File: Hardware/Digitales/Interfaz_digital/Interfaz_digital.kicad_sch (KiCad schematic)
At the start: 47 parts, among them J0_1 Screw_Terminal_01x03, J0_2 Screw_Terminal_01x03, J0_3 Screw_Terminal_01x03, J1-1 Screw_Terminal_01x01, J1-2 Screw_Terminal_01x01, J2-1 Screw_Terminal_01x01, J2-2 Screw_Terminal_01x01, J3-1 Screw_Terminal_01x01, J3-2 Screw_Terminal_01x01, J4-1 Screw_Terminal_01x01, J4-2 Screw_Terminal_01x01, J5-1 Screw_Terminal_01x01, J5-2 Screw_Terminal_01x01, J6-1 Screw_Terminal_01x01, J6-2 Screw_Terminal_01x01, J7-1 Screw_Terminal_01x01, J7-2 Screw_Terminal_01x01, J8-1 Screw_Terminal_01x01, J8-2 Screw_Terminal_01x01, J9_1 Screw_Terminal_01x03, J9_2 Screw_Terminal_01x03, J9_3 Screw_Terminal_01x03, J9_4 Screw_Terminal_01x03, U1 TLP521-1, U2 TLP521-1, U3 TLP521-1, U4 TLP521-1, U5 TLP521-1, U6 TLP521-1, U7 TLP521-1, U8 TLP521-1

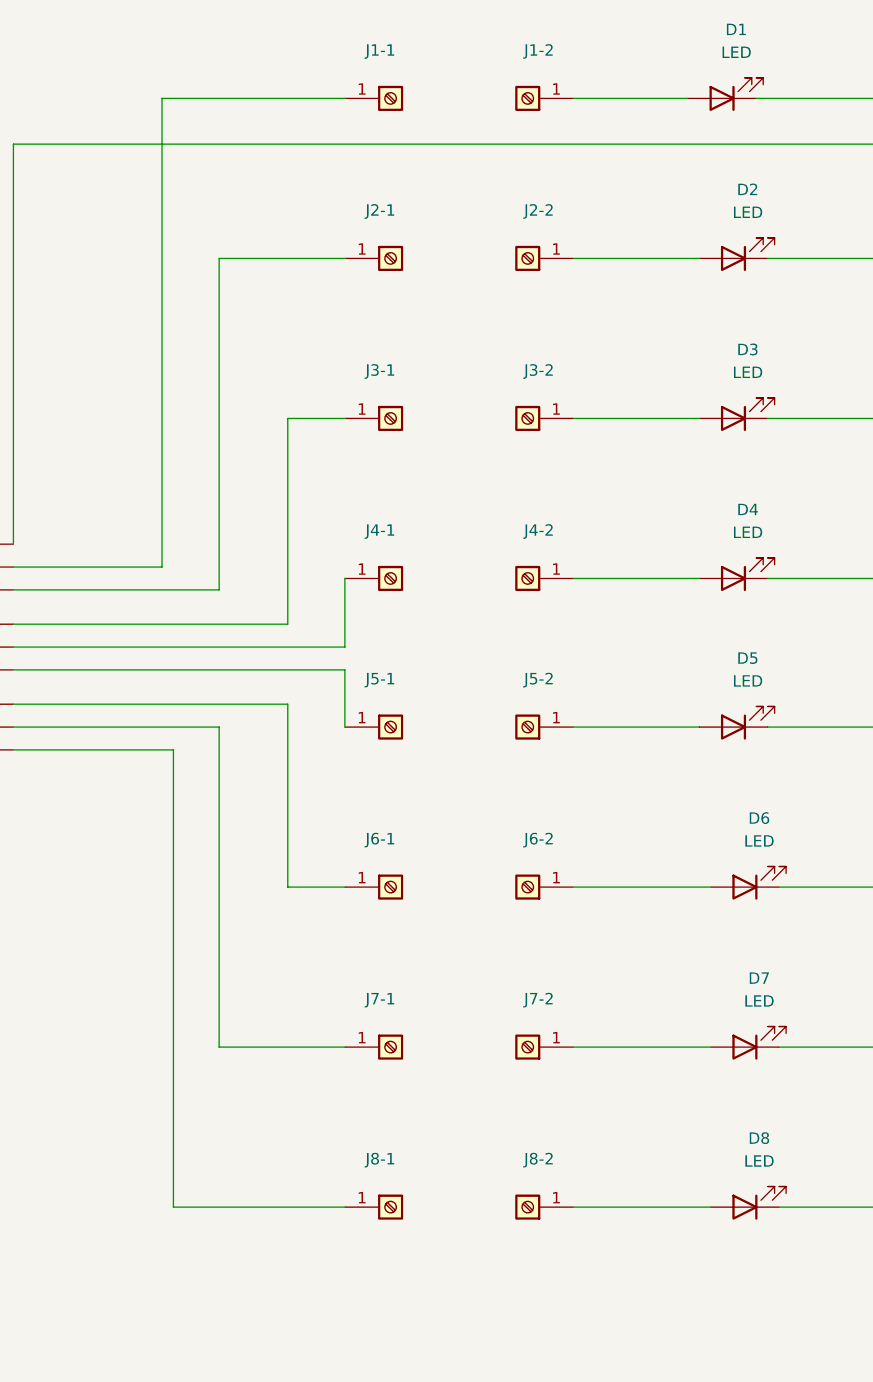
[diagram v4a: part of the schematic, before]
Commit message: Ajustes a las interfaces digital y analogica
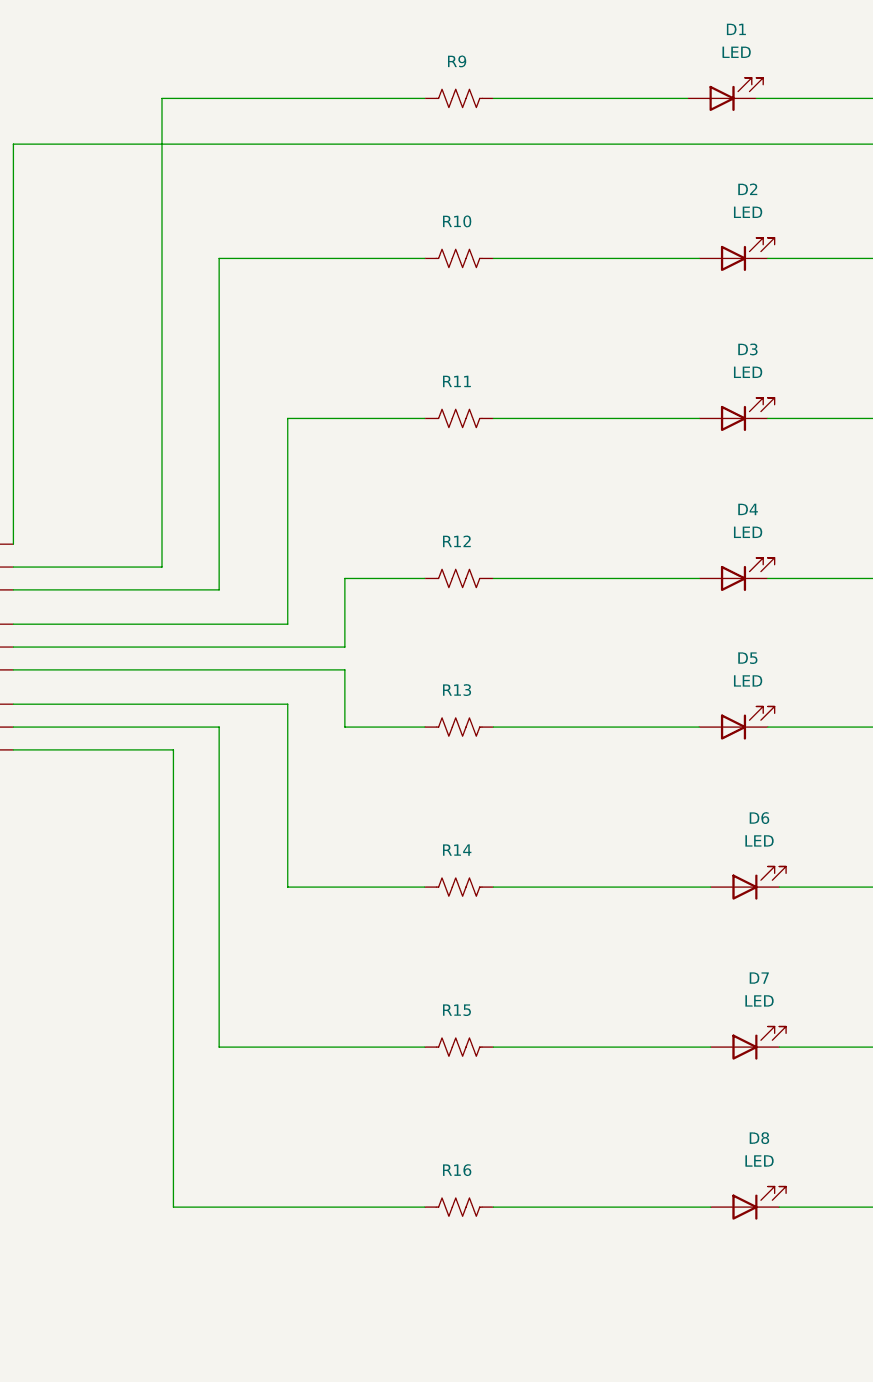
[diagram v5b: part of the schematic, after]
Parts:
- removed J1-1, J1-2, J2-1, J2-2, J3-1, J3-2, J4-1, J4-2, J5-1, J5-2, J6-1, J6-2, J7-1, J7-2, J8-1, J8-2: Screw_Terminal_01x01, TerminalBlock_MetzConnect:TerminalBlock_MetzConnect_360271_1x01_Horizontal_ScrewM3.0_Boxed, symbol Connector:Screw_Terminal_01x01
- added R10, R11, R12, R13, R14, R15, R16, R9: R_US, Resistor_THT:R_Axial_DIN0207_L6.3mm_D2.5mm_P7.62mm_Horizontal, symbol Device:R_US
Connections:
- net at D3.2 (A): now also R11.2
- net at J0_3.2 (Pin_2): now also R15.1
- net at J0_2.1 (Pin_1): now also R11.1
- net at J0_1.2 (Pin_2): now also R9.1
- net at J0_1.3 (Pin_3): now also R10.1
- net at J0_3.1 (Pin_1): now also R14.1
- net at J0_2.2 (Pin_2): now also R12.1
- net at J0_2.3 (Pin_3): now also R13.1
- net at D4.2 (A): now also R12.2
- net at D8.2 (A): now also R16.2
- net at D2.2 (A): now also R10.2
- net at D1.2 (A): now also R9.2
- net at J0_3.3 (Pin_3): now also R16.1
- net at D5.2 (A): now also R13.2
- net at D6.2 (A): now also R14.2
- net at D7.2 (A): now also R15.2
